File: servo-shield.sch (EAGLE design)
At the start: 32 parts, among them K1 PIN20X2

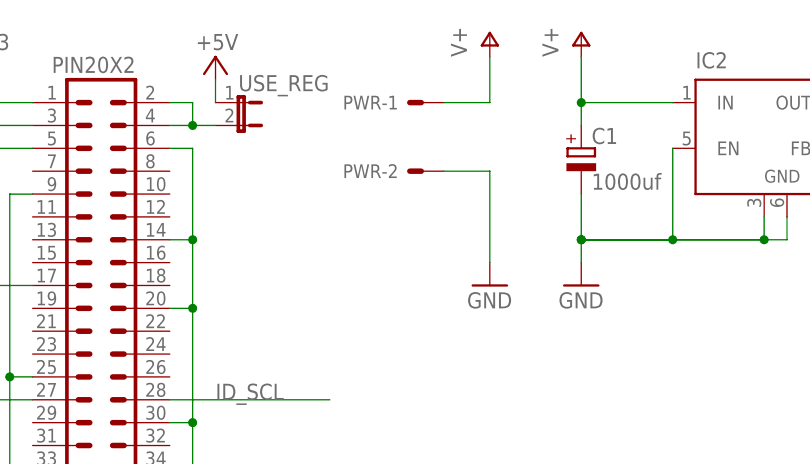
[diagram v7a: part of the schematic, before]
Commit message: Rejigged to add passthru power connector
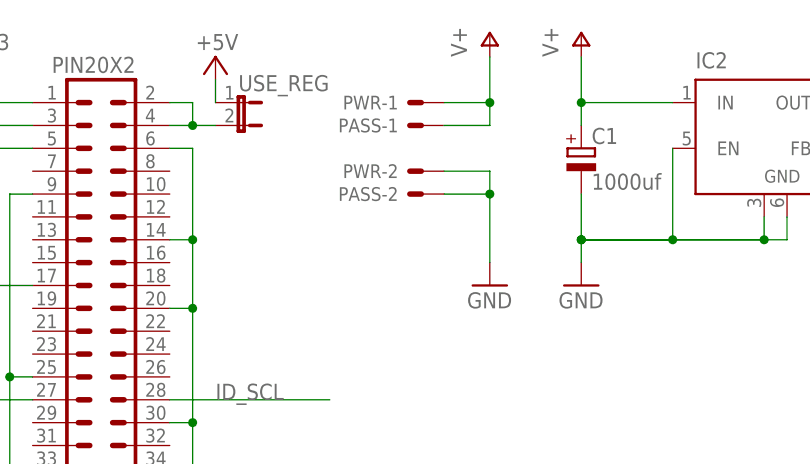
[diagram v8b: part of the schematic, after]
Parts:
- added PASS: 22-05-7028-02, con-molex:22-05-7028-02
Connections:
- net GND: now also PASS-2.S
- net V+: now also PASS-1.S
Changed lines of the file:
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@@
 <part name="FRAME1" library="frames" deviceset="DINA4_L" device=""/>
 <part name="USE_REG" library="jumper" deviceset="JP1E" device=""/>
+<part name="PASS" library="con-molex" deviceset="22-?-02" device="05-7028"/>
 </parts>
 <sheets>
@@
 <instance part="FRAME1" gate="G$2" x="0" y="0"/>
 <instance part="USE_REG" gate="A" x="66.04" y="170.18" rot="R270"/>
+<instance part="PASS" gate="-1" x="86.36" y="167.64" smashed="yes" rot="R180">
+<attribute name="NAME" x="83.82" y="168.402" size="1.524" layer="95" rot="R180"/>
+</instance>
+<instance part="PASS" gate="-2" x="86.36" y="160.02" rot="R180"/>
 </instances>
 <busses>
@@
 <segment>
 <wire x1="88.9" y1="162.56" x2="93.98" y2="162.56" width="0.1524" layer="91"/>
-<wire x1="93.98" y1="162.56" x2="93.98" y2="152.4" width="0.1524" layer="91"/>
+<wire x1="93.98" y1="162.56" x2="93.98" y2="160.02" width="0.1524" layer="91"/>
 <pinref part="GND11" gate="1" pin="GND"/>
 <pinref part="PWR" gate="-2" pin="S"/>
+<wire x1="93.98" y1="160.02" x2="93.98" y2="152.4" width="0.1524" layer="91"/>
+<wire x1="88.9" y1="160.02" x2="93.98" y2="160.02" width="0.1524" layer="91"/>
+<pinref part="PASS" gate="-2" pin="S"/>
+<junction x="93.98" y="160.02"/>
 </segment>
 <segment>
@@
 <wire x1="93.98" y1="170.18" x2="93.98" y2="175.26" width="0.1524" layer="91"/>
 <pinref part="PWR" gate="-1" pin="S"/>
-</segment>
-<segment>
+<junction x="93.98" y="170.18"/>
+<wire x1="88.9" y1="167.64" x2="93.98" y2="167.64" width="0.1524" layer="91"/>
+<pinref part="PASS" gate="-1" pin="S"/>
+<wire x1="93.98" y1="167.64" x2="93.98" y2="170.18" width="0.1524" layer="91"/>
+</segment>
+<segment>
